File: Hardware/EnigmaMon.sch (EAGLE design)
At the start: 49 parts, among them IC1 4051N, IC2 TLC5940, T1 BC548, T2 BC548, T3 BC548, T4 BC548, T5 BC548, T6 BC548, T8 BC548, T9 BC548

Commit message: Added VMR
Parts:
- added C1, C3: 10uF, rcl:CPOL-EUE2.5-6
- added INPUT_PWR: (no value), EnigmaMon:PINHD-1X2
- added LM7805: (no value), EnigmaMon:78XXL
- added R13, R14: 220, rcl:R-EU_0204/7
- added U$4: DTS6, EnigmaMon:DTS6
- PWR: device EnigmaMon:PINHD-1X2 -> EnigmaMon:LED3MM
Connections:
- new net N$12: R14.2, U$4.S, U$4.S@1
- new net N$7: PWR.C, R13.2
- new net RESET: R14.1, U$1.RESET
- net +12V: now also C1.+, INPUT_PWR.2, LM7805.IN; no longer PWR.2
- net GND: now also C1.-, C3.-, INPUT_PWR.1, LM7805.GND, R13.1, U$4.P, U$4.P@1; no longer PWR.1
- net VCC: now also C3.+, LM7805.OUT, PWR.A
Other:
- note added: "Fan Control"
- note added: "Power"
- moved on the sheet: C2, D1, D2, D3, D4, D5, D6, D8, D9, FAN1, FAN2, FAN3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

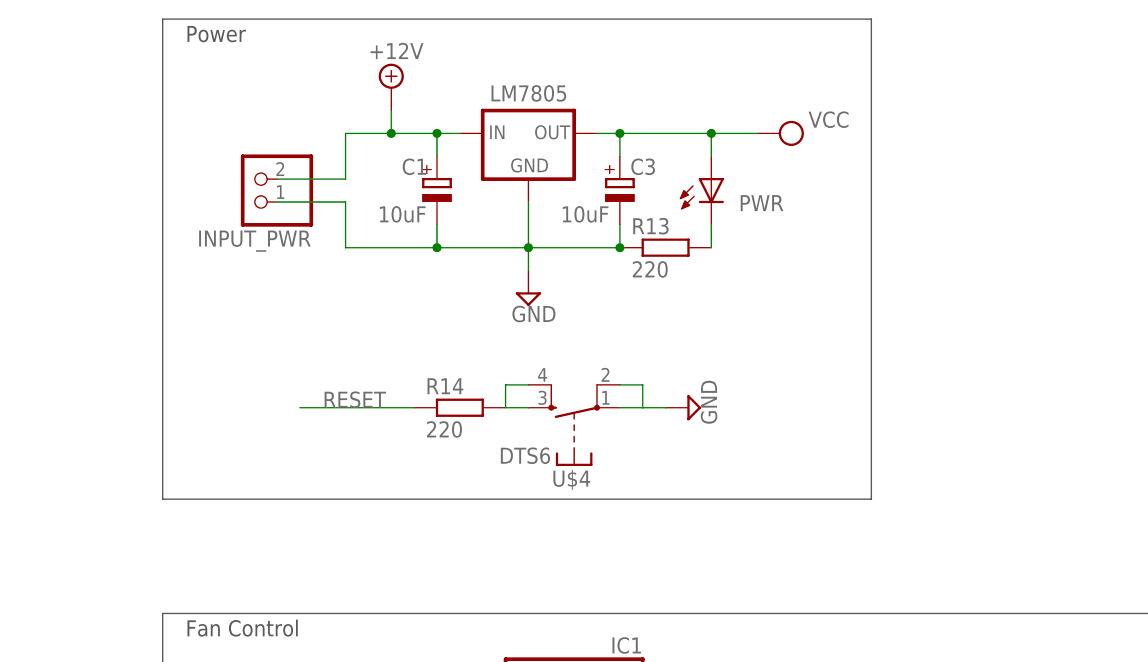
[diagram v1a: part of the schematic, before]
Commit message: Fixed error with reset switch
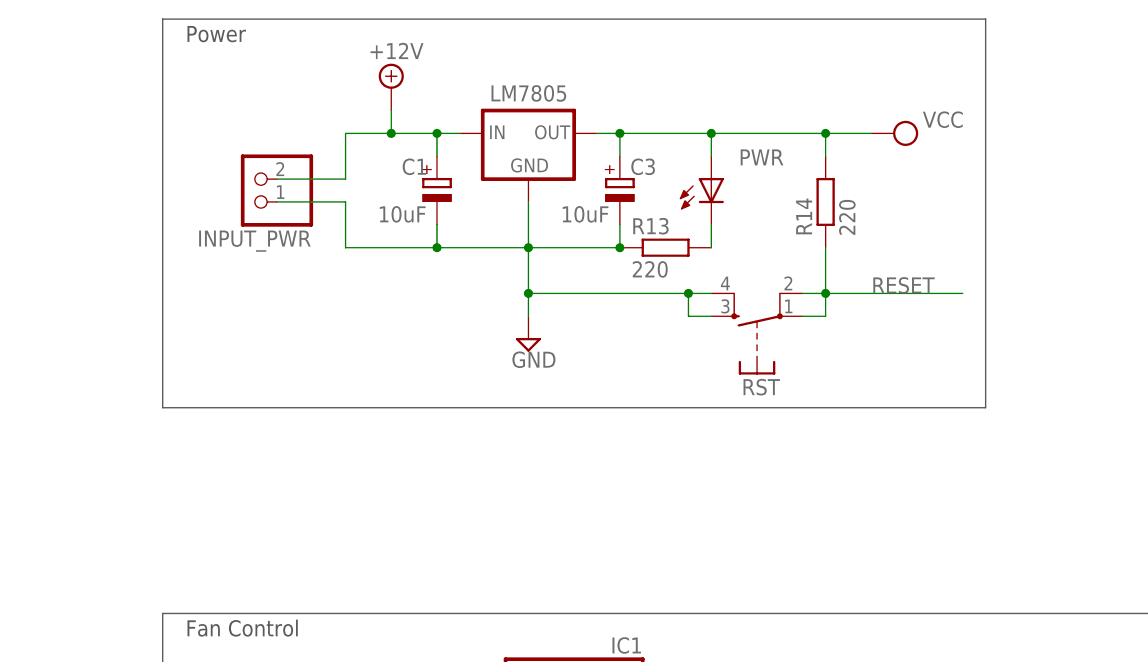
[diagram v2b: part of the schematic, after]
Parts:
- removed U$4: DTS6, EnigmaMon:DTS6
- added RST: DTS6, EnigmaMon:DTS6
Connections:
- removed net N$12: R14.2, U$4.S, U$4.S@1
- net GND: now also RST.S, RST.S@1; no longer U$4.P, U$4.P@1
- net RESET: now also RST.P, RST.P@1
- net VCC: now also R14.2
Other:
- moved on the sheet: R14
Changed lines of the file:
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@@
 <part name="R13" library="rcl" deviceset="R-EU_" device="0204/7" value="220"/>
 <part name="SUPPLY9" library="EnigmaMon" deviceset="+12V" device=""/>
-<part name="SUPPLY10" library="EnigmaMon" deviceset="GND" device=""/>
 <part name="R14" library="rcl" deviceset="R-EU_" device="0204/7" value="220"/>
-<part name="U$4" library="EnigmaMon" deviceset="DTS6" device=""/>
+<part name="RST" library="EnigmaMon" deviceset="DTS6" device=""/>
 </parts>
 <sheets>
@@
 <wire x1="17.78" y1="-45.72" x2="17.78" y2="99.06" width="0.1524" layer="97"/>
 <text x="20.32" y="96.52" size="1.778" layer="97">Fan Control</text>
-<wire x1="17.78" y1="165.1" x2="96.52" y2="165.1" width="0.1524" layer="97"/>
-<wire x1="96.52" y1="165.1" x2="96.52" y2="111.76" width="0.1524" layer="97"/>
-<wire x1="96.52" y1="111.76" x2="17.78" y2="111.76" width="0.1524" layer="97"/>
-<wire x1="17.78" y1="111.76" x2="17.78" y2="165.1" width="0.1524" layer="97"/>
+<wire x1="17.78" y1="165.1" x2="109.22" y2="165.1" width="0.1524" layer="97"/>
+<wire x1="109.22" y1="165.1" x2="109.22" y2="121.92" width="0.1524" layer="97"/>
+<wire x1="109.22" y1="121.92" x2="17.78" y2="121.92" width="0.1524" layer="97"/>
+<wire x1="17.78" y1="121.92" x2="17.78" y2="165.1" width="0.1524" layer="97"/>
 <text x="20.32" y="162.56" size="1.778" layer="97">Power</text>
 </plain>
@@
 <attribute name="VALUE" x="60.96" y="142.24" size="1.778" layer="96"/>
 </instance>
-<instance part="SUPPLY34" gate="GND" x="58.42" y="134.62"/>
-<instance part="SUPPLY36" gate="G$1" x="86.36" y="152.4" smashed="yes" rot="R270">
-<attribute name="VALUE" x="89.535" y="153.035" size="1.778" layer="96"/>
+<instance part="SUPPLY34" gate="GND" x="58.42" y="129.54"/>
+<instance part="SUPPLY36" gate="G$1" x="99.06" y="152.4" smashed="yes" rot="R270">
+<attribute name="VALUE" x="102.235" y="153.035" size="1.778" layer="96"/>
 </instance>
 <instance part="C1" gate="G$1" x="48.26" y="147.32" smashed="yes">
@@
 </instance>
 <instance part="PWR" gate="G$1" x="78.74" y="147.32" smashed="yes">
-<attribute name="NAME" x="81.788" y="143.764" size="1.778" layer="95"/>
+<attribute name="NAME" x="81.788" y="148.844" size="1.778" layer="95"/>
 <attribute name="VALUE" x="84.455" y="142.748" size="1.778" layer="96" rot="R90"/>
 </instance>
 <instance part="R13" gate="G$1" x="73.66" y="139.7"/>
 <instance part="SUPPLY9" gate="+12V" x="43.18" y="157.48"/>
-<instance part="SUPPLY10" gate="GND" x="76.2" y="121.92" rot="R90"/>
-<instance part="R14" gate="G$1" x="50.8" y="121.92"/>
-<instance part="U$4" gate="G$1" x="63.5" y="121.92" rot="R90"/>
+<instance part="R14" gate="G$1" x="91.44" y="144.78" rot="R90"/>
+<instance part="RST" gate="G$1" x="83.82" y="132.08" rot="R90"/>
 </instances>
 <busses>
@@
 <pinref part="SUPPLY34" gate="GND" pin="GND"/>
 <pinref part="C1" gate="G$1" pin="-"/>
-<wire x1="58.42" y1="139.7" x2="58.42" y2="137.16" width="0.1524" layer="91"/>
+<wire x1="58.42" y1="139.7" x2="58.42" y2="134.62" width="0.1524" layer="91"/>
+<wire x1="58.42" y1="134.62" x2="58.42" y2="132.08" width="0.1524" layer="91"/>
 <wire x1="48.26" y1="142.24" x2="48.26" y2="139.7" width="0.1524" layer="91"/>
 <wire x1="48.26" y1="139.7" x2="58.42" y2="139.7" width="0.1524" layer="91"/>
@@
 <pinref part="INPUT_PWR" gate="G$1" pin="1"/>
 <junction x="48.26" y="139.7"/>
-</segment>
-<segment>
-<wire x1="68.58" y1="124.46" x2="71.12" y2="124.46" width="0.1524" layer="91"/>
-<wire x1="71.12" y1="124.46" x2="71.12" y2="121.92" width="0.1524" layer="91"/>
-<wire x1="71.12" y1="121.92" x2="68.58" y2="121.92" width="0.1524" layer="91"/>
-<wire x1="71.12" y1="121.92" x2="73.66" y2="121.92" width="0.1524" layer="91"/>
-<pinref part="SUPPLY10" gate="GND" pin="GND"/>
-<pinref part="U$4" gate="G$1" pin="P"/>
-<pinref part="U$4" gate="G$1" pin="P@1"/>
+<pinref part="RST" gate="G$1" pin="S@1"/>
+<wire x1="78.74" y1="134.62" x2="76.2" y2="134.62" width="0.1524" layer="91"/>
+<pinref part="RST" gate="G$1" pin="S"/>
+<wire x1="76.2" y1="134.62" x2="76.2" y2="132.08" width="0.1524" layer="91"/>
+<wire x1="76.2" y1="132.08" x2="78.74" y2="132.08" width="0.1524" layer="91"/>
+<wire x1="76.2" y1="134.62" x2="58.42" y2="134.62" width="0.1524" layer="91"/>
+<junction x="58.42" y="134.62"/>
+<junction x="76.2" y="134.62"/>
 </segment>
 </net>
@@
 <pinref part="C3" gate="G$1" pin="+"/>
 <wire x1="68.58" y1="152.4" x2="78.74" y2="152.4" width="0.1524" layer="91"/>
-<wire x1="78.74" y1="152.4" x2="83.82" y2="152.4" width="0.1524" layer="91"/>
+<wire x1="78.74" y1="152.4" x2="91.44" y2="152.4" width="0.1524" layer="91"/>
+<wire x1="91.44" y1="152.4" x2="96.52" y2="152.4" width="0.1524" layer="91"/>
 <wire x1="66.04" y1="152.4" x2="68.58" y2="152.4" width="0.1524" layer="91"/>
 <wire x1="68.58" y1="152.4" x2="68.58" y2="149.86" width="0.1524" layer="91"/>
@@
 <junction x="68.58" y="152.4"/>
 <junction x="78.74" y="152.4"/>
+<pinref part="R14" gate="G$1" pin="2"/>
+<wire x1="91.44" y1="152.4" x2="91.44" y2="149.86" width="0.1524" layer="91"/>
+<junction x="91.44" y="152.4"/>
 </segment>
 </net>
@@
 </segment>
 </net>
-<net name="N$12" class="0">
-<segment>
-<pinref part="R14" gate="G$1" pin="2"/>
-<wire x1="58.42" y1="124.46" x2="55.88" y2="124.46" width="0.1524" layer="91"/>
-<wire x1="55.88" y1="124.46" x2="55.88" y2="121.92" width="0.1524" layer="91"/>
-<wire x1="55.88" y1="121.92" x2="58.42" y2="121.92" width="0.1524" layer="91"/>
-<pinref part="U$4" gate="G$1" pin="S"/>
-<pinref part="U$4" gate="G$1" pin="S@1"/>
-</segment>
-</net>
 <net name="RESET" class="0">
 <segment>
 <pinref part="R14" gate="G$1" pin="1"/>
-<wire x1="45.72" y1="121.92" x2="33.02" y2="121.92" width="0.1524" layer="91"/>
-<label x="35.56" y="121.92" size="1.778" layer="95"/>
-</segment>
-<segment>
+<wire x1="91.44" y1="134.62" x2="106.68" y2="134.62" width="0.1524" layer="91"/>
+<label x="96.52" y="134.62" size="1.778" layer="95"/>
+<pinref part="RST" gate="G$1" pin="P"/>
+<wire x1="91.44" y1="139.7" x2="91.44" y2="134.62" width="0.1524" layer="91"/>
+<wire x1="91.44" y1="134.62" x2="91.44" y2="132.08" width="0.1524" layer="91"/>
+<wire x1="91.44" y1="132.08" x2="88.9" y2="132.08" width="0.1524" layer="91"/>
+<pinref part="RST" gate="G$1" pin="P@1"/>
+<wire x1="88.9" y1="134.62" x2="91.44" y2="134.62" width="0.1524" layer="91"/>
+<junction x="91.44" y="134.62"/>
+</segment>
+<segment>

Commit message: Couple of minor updates
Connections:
- net GND: now also IC2G$1.OUT10, IC2G$1.OUT11, IC2G$1.OUT12, IC2G$1.OUT13, IC2G$1.OUT14, IC2G$1.OUT15, IC2G$1.OUT9
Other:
- note added: "Arduino Connections"
- note added: "Fan Interface"
- note added: "Fan PWM Control"
- note added: "Fan Tachometer Control"
- note removed: "Fan Control"
- moved on the sheet: C1, C2, C3, D1, D2, D3, D4, D5, D6, D8, D9, FAN1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
